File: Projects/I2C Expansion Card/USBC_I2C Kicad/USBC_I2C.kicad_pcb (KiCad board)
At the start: 2 copper layers, 26 x 30 mm, 12 parts, among them U1 MCP2221A

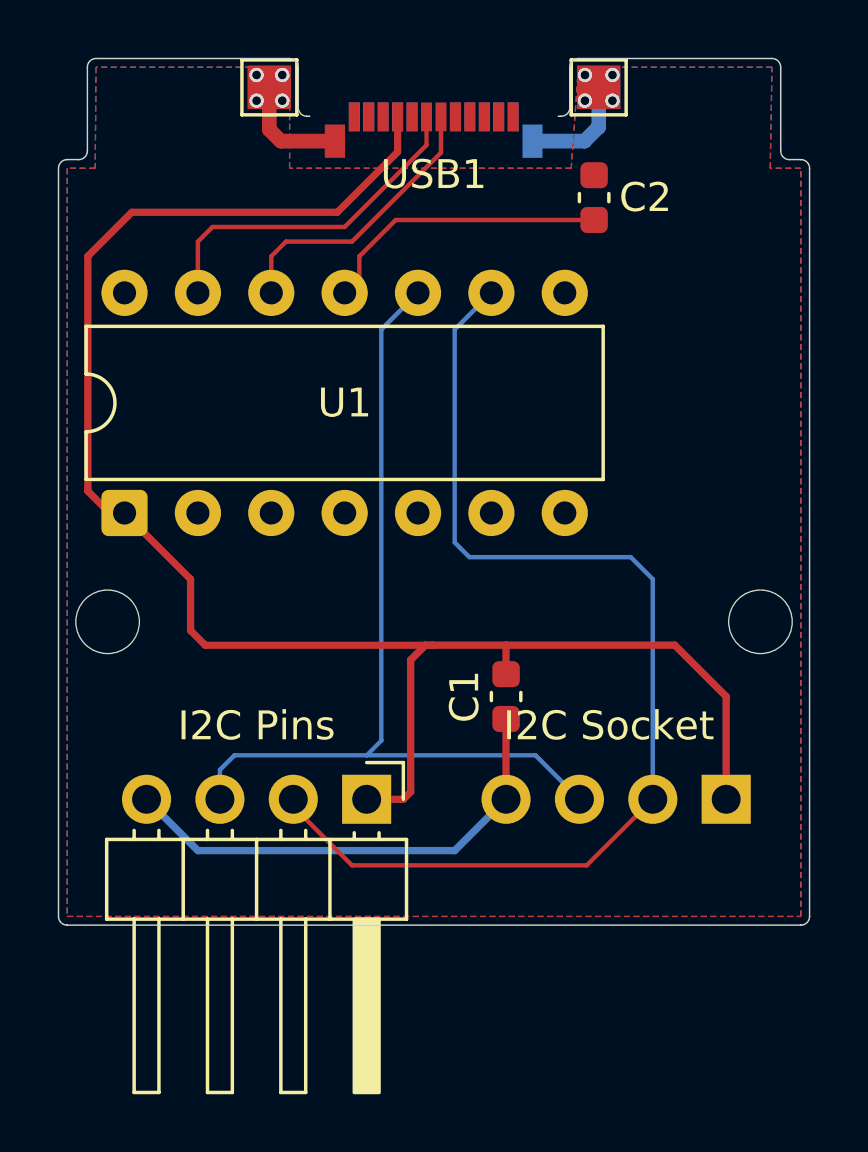
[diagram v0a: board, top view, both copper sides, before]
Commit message: Swapped to SMD chip
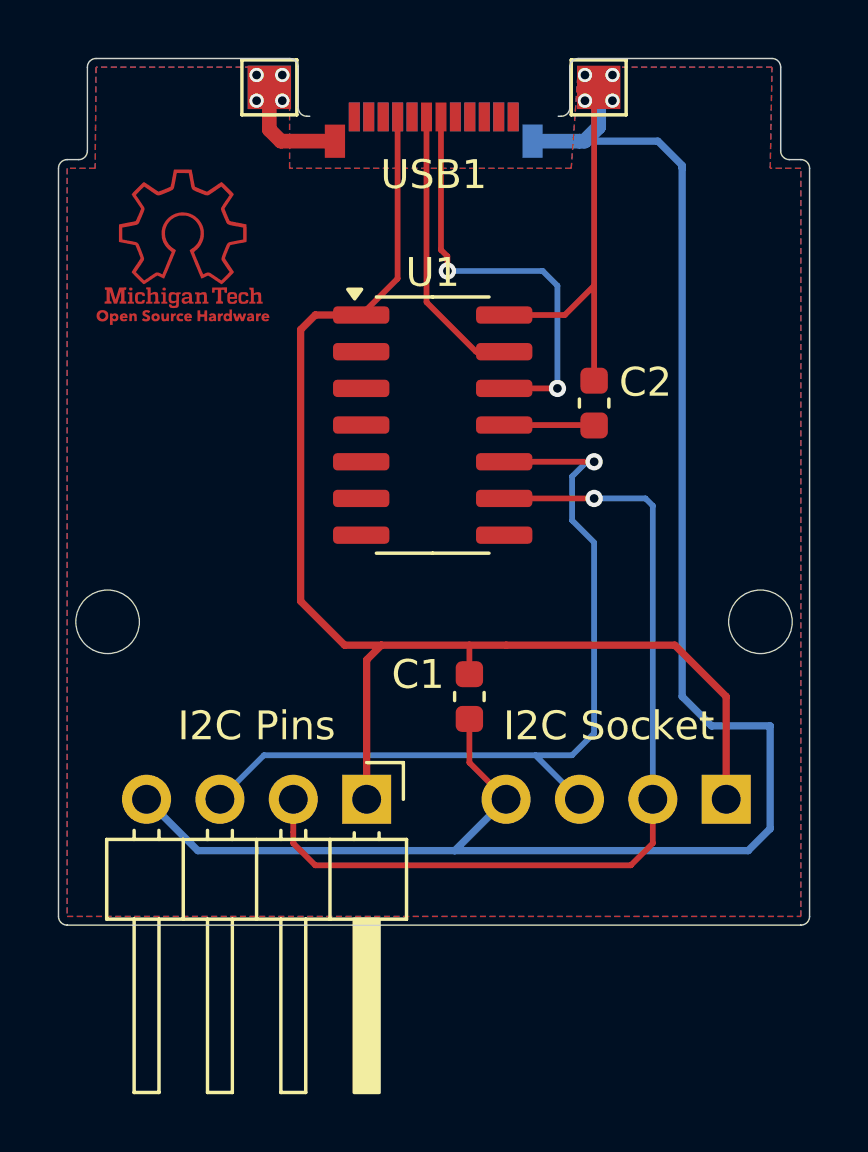
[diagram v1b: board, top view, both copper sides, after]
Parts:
- removed TP4: TestPoint, TestPoint:TestPoint_Pad_1.5x1.5mm
- added G***: LOGO, LOGO, F.Cu at (88.1, 63.8)
- U1: value MCP2221A -> MCP2221AxSL; footprint Package_DIP:DIP-14_W7.62mm -> Package_SO:SOIC-14_3.9x8.7mm_P1.27mm
- moved U1 11.1 mm to (96.8, 69.8), turned to 0 degrees
- moved C2 7.11 mm to (102.4, 69.1)
- moved C1 1.27 mm to (98.0, 79.2)
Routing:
- net GND: track 24.4 -> 79.2 mm
- net 5V: track 59.4 -> 45.3 mm
- net SDA: track 38.7 -> 31.5 mm, vias 0 -> 1
- net Net-(U1-VUSB): track 10.1 -> 3.12 mm
- net Net-(U1-D-): track 9.86 -> 14.8 mm, vias 0 -> 2
- net Net-(U1-D+): track 12.0 -> 9.81 mm
- net SCL: track 31.0 -> 29.3 mm, vias 0 -> 1

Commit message: Added capacitor values
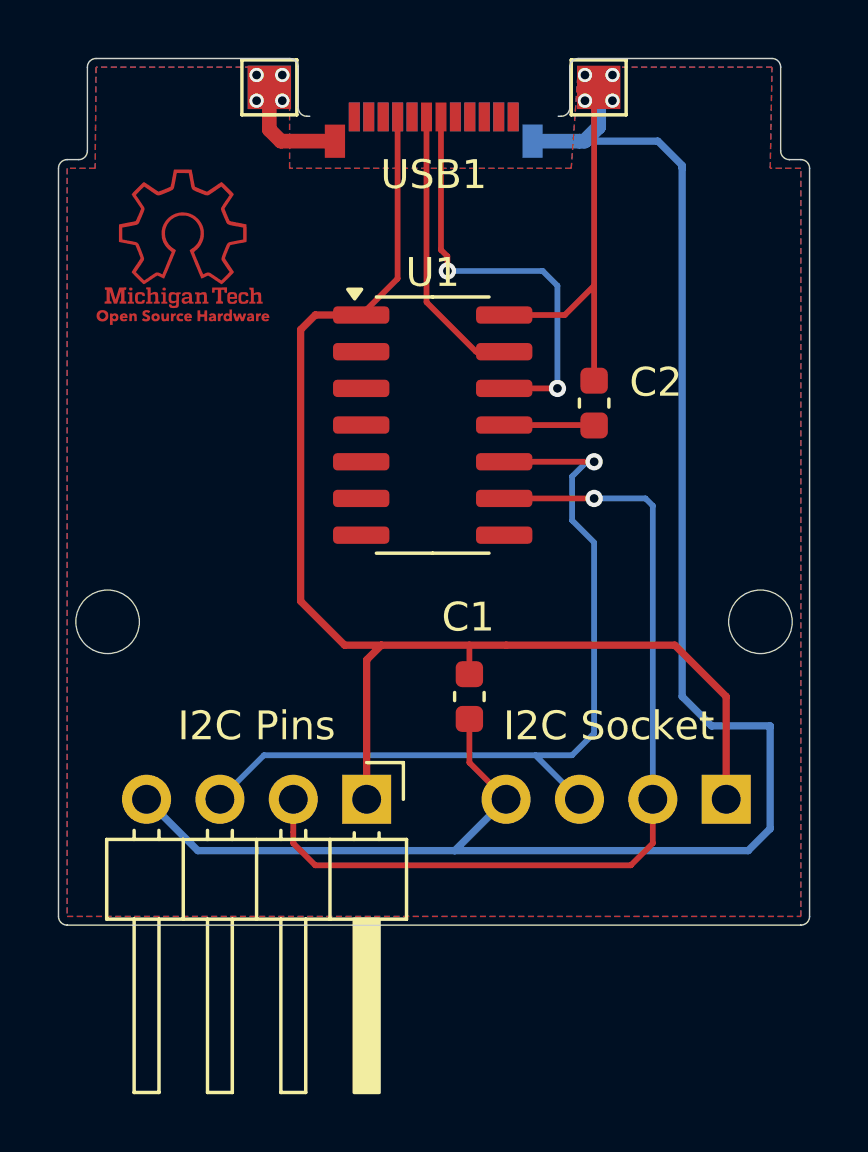
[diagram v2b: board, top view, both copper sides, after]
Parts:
- C1: value C -> .47uF
- C2: value C -> .22uF
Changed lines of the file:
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@@
 		(tags "capacitor")
 		(property "Reference" "C1"
-			(at 0.762 -1.778 180)
+			(at 2.748 -0.044 180)
 			(layer "F.SilkS")
 			(effects
@@
 			)
 		)
-		(property "Value" "C"
-			(at -0.762 -1.778 180)
+		(property "Value" ".47uF"
+			(at 0.748 -3.044 180)
 			(layer "F.Fab")
 			(effects
@@
 		(tags "capacitor")
 		(property "Reference" "C2"
-			(at -0.718 -1.778 0)
+			(at -0.718 -2.138 0)
 			(layer "F.SilkS")
 			(effects
@@
 			)
 		)
-		(property "Value" "C"
-			(at 0.762 -1.778 0)
-			(layer "F.Fab")
-			(effects
+		(property "Value" ".22uF"
+			(at 0.912 -3.138 0)
+			(layer "F.Fab")
+			(effects

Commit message: Added Impedance Matching and added 5V Plane
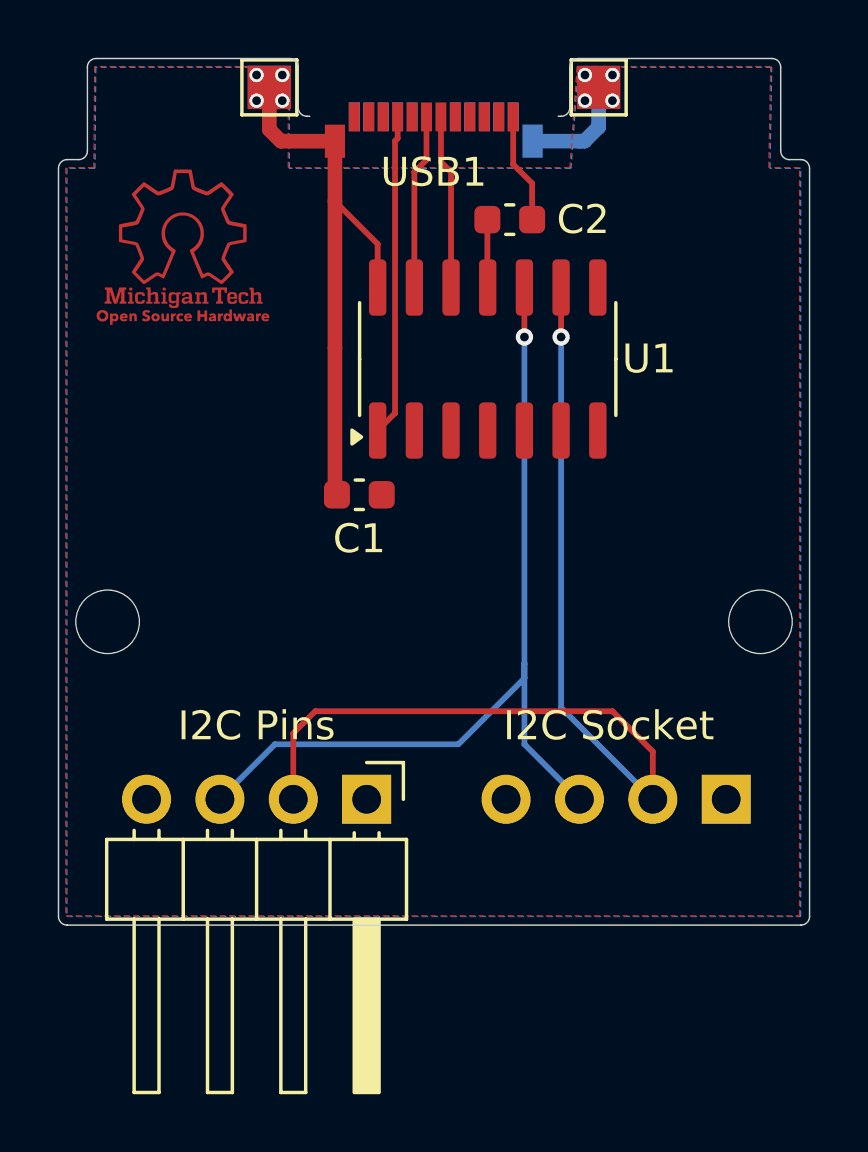
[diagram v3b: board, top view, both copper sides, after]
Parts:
- moved C1 7.96 mm to (94.2, 72.3), turned to 180 degrees
- moved C2 6.99 mm to (99.4, 62.7), turned to 180 degrees
- moved U1 2.98 mm to (98.7, 67.6), turned to 90 degrees
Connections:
- C1 pad 1: GND -> 5V
- C1 pad 2: 5V -> GND
- I2C Pins pad 1: (no net) -> 5V
- I2C Pins pad 2: (no net) -> SDA
- I2C Pins pad 3: (no net) -> SCL
- I2C Pins pad 4: (no net) -> GND
- I2C Socket pad 1: (no net) -> 5V
- I2C Socket pad 2: (no net) -> SDA
- I2C Socket pad 3: (no net) -> SCL
- I2C Socket pad 4: (no net) -> GND
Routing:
- net GND: track 79.2 -> 27.9 mm
- net 5V: track 45.3 -> 11.1 mm
- net Net-(U1-D-): track 14.8 -> 6.05 mm, vias 2 -> 0
- net SDA: track 31.5 -> 36.3 mm
- net Net-(U1-D+): track 9.81 -> 6.08 mm
- net SCL: track 29.3 -> 31.3 mm
- net Net-(U1-VUSB): track 3.12 -> 2.36 mm
- added copper zone on F.Cu, net 5V
- removed copper zone on F.Cu, net GND

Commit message: Fixed trace routing on dual output card
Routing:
- net SCL: track 31.3 -> 34.3 mm
- net SDA: track 36.3 -> 37.6 mm
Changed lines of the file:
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@@
 	)
 	(segment
-		(start 99.949 78.613)
-		(end 99.949 78.105)
+		(start 91.313 80.899)
+		(end 89.408 82.804)
 		(width 0.2)
 		(layer "B.Cu")
@@
 	)
 	(segment
-		(start 99.949 78.105)
-		(end 99.949 80.899)
+		(start 103.5 77.5)
+		(end 100.101 80.899)
 		(width 0.2)
 		(layer "B.Cu")
@@
 	)
 	(segment
-		(start 89.408 82.804)
-		(end 91.313 80.899)
+		(start 103.5 68.5)
+		(end 103.5 77.5)
 		(width 0.2)
 		(layer "B.Cu")
@@
 	)
 	(segment
-		(start 97.663 80.899)
-		(end 99.949 78.613)
+		(start 99.949 67.449)
+		(end 100.5 68)
+		(width 0.2)
+		(layer "B.Cu")
+		(net 7)
+	)
+	(segment
+		(start 99.949 66.802)
+		(end 99.949 67.449)
+		(width 0.2)
+		(layer "B.Cu")
+		(net 7)
+	)
+	(segment
+		(start 103 68)
+		(end 103.5 68.5)
+		(width 0.2)
+		(layer "B.Cu")
+		(net 7)
+	)
+	(segment
+		(start 100.101 80.899)
+		(end 91.313 80.899)
 		(width 0.2)
 		(layer "B.Cu")
@@
 	)
 	(segment
-		(start 91.313 80.899)
-		(end 97.663 80.899)
-		(width 0.2)
-		(layer "B.Cu")
-		(net 7)
-	)
-	(segment
-		(start 99.949 66.802)
-		(end 99.949 78.105)
+		(start 100.5 68)
+		(end 103 68)
 		(width 0.2)
 		(layer "B.Cu")
@@
 	)
 	(segment
-		(start 101.219 79.629)
+		(start 103.302 66.802)
+		(end 104.5 68)
+		(width 0.2)
+		(layer "B.Cu")
+		(net 9)
+	)
+	(segment
+		(start 104.5 68)
+		(end 104.5 82.698)
+		(width 0.2)
+		(layer "B.Cu")
+		(net 9)
+	)
+	(segment
+		(start 104.5 82.698)
 		(end 104.394 82.804)
 		(width 0.2)
@@
 	(segment
 		(start 101.219 66.802)
-		(end 101.219 79.629)
+		(end 103.302 66.802)
 		(width 0.2)
 		(layer "B.Cu")

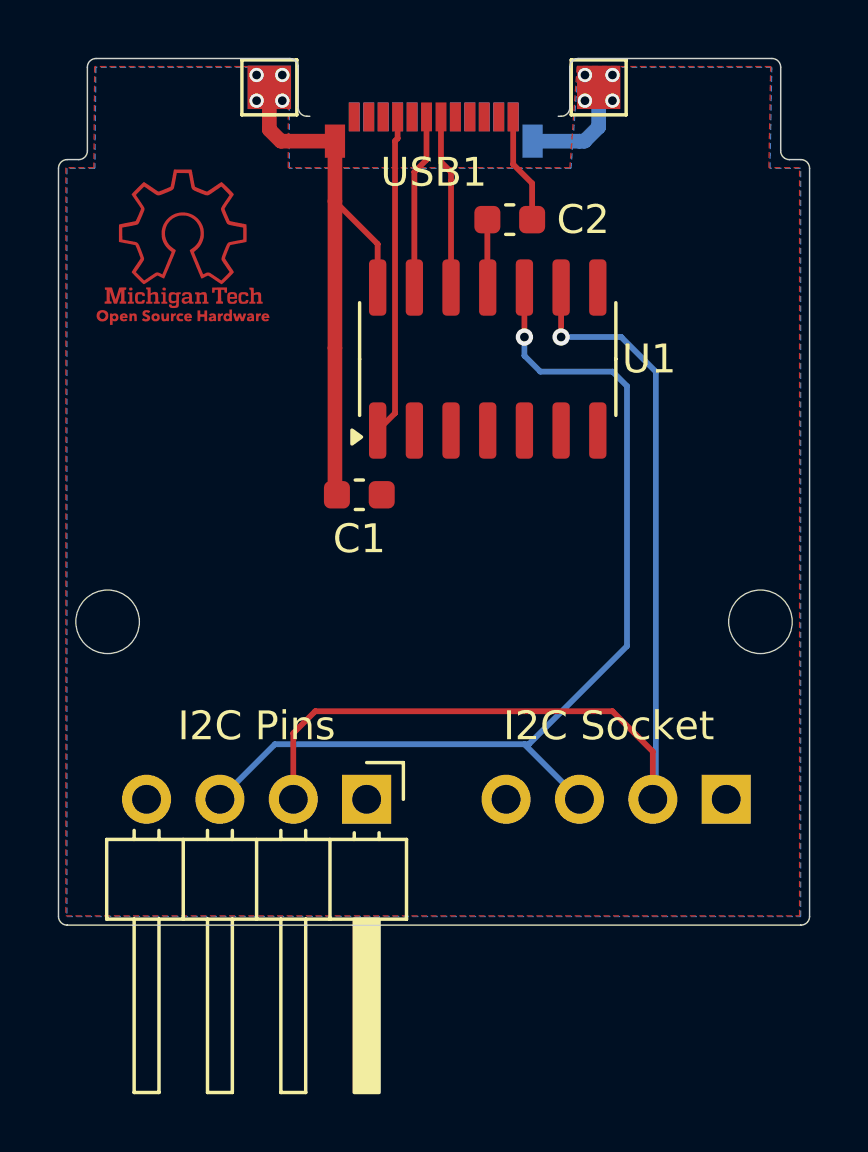
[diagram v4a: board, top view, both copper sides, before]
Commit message: Reworked pcb to put everything on one board
Merged the 3 versions into one, added through hole cap holes, added uart switch, fixed the pcb edge
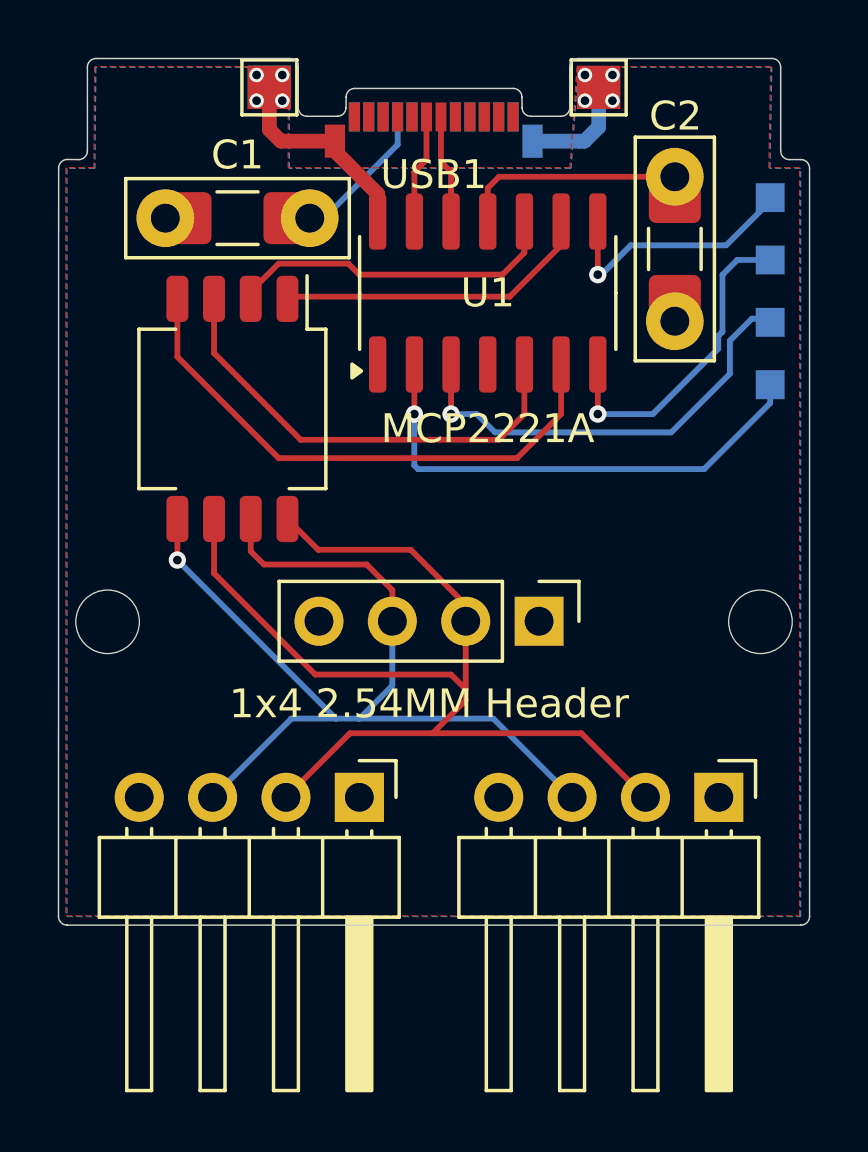
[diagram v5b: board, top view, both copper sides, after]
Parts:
- removed G***: LOGO, LOGO
- removed I2C Pins: I2C Pins, Connector_PinHeader_2.54mm:PinHeader_1x04_P2.54mm_Horizontal
- removed I2C Socket: PinSocket_1x04_P2.54mm_Horizontal, Connector_PinSocket_2.54mm:PinSocket_1x04_P2.54mm_Horizontal
- added REF**: PinHeader_1x04_P2.54mm_Horizontal, Connector_PinHeader_2.54mm:PinHeader_1x04_P2.54mm_Horizontal, F.Cu at (94.2, 82.7)
- added REF**: TestPoint_Pad_1.0x1.0mm, TestPoint:TestPoint_Pad_1.0x1.0mm, B.Cu at (108.5, 64.1)
- added REF**: C_Disc_D7.5mm_W2.5mm_P5.00mm, Capacitor_THT:C_Disc_D7.5mm_W2.5mm_P5.00mm, F.Cu at (92.5, 62.7)
- added REF**: SW_DIP_SPSTx04_Slide_Copal_CHS-04B_W7.62mm_P1.27mm, Button_Switch_SMD:SW_DIP_SPSTx04_Slide_Copal_CHS-04B_W7.62mm_P1.27mm, F.Cu at (89.8, 69.3)
- added REF**: PinHeader_1x04_P2.54mm_Vertical, Connector_PinHeader_2.54mm:PinHeader_1x04_P2.54mm_Vertical, F.Cu at (100.5, 76.6)
- added REF**: C_Disc_D7.5mm_W2.5mm_P5.00mm, Capacitor_THT:C_Disc_D7.5mm_W2.5mm_P5.00mm, F.Cu at (105.2, 61.3)
- added REF**: PinHeader_1x04_P2.54mm_Horizontal, Connector_PinHeader_2.54mm:PinHeader_1x04_P2.54mm_Horizontal, F.Cu at (106.7, 82.7)
- added REF**: TestPoint_Pad_1.0x1.0mm, TestPoint:TestPoint_Pad_1.0x1.0mm, B.Cu at (108.5, 62.0)
- added REF**: TestPoint_Pad_1.0x1.0mm, TestPoint:TestPoint_Pad_1.0x1.0mm, B.Cu at (108.5, 68.5)
- added REF**: TestPoint_Pad_1.0x1.0mm, TestPoint:TestPoint_Pad_1.0x1.0mm, B.Cu at (108.5, 66.3)
- C1: value .47uF -> 0.47uF; footprint Capacitor_SMD:C_0603_1608Metric -> Capacitor_SMD:C_1206_3216Metric_Pad1.33x1.80mm_HandSolder
- C2: value .22uF -> 0.22uF; footprint Capacitor_SMD:C_0603_1608Metric -> Capacitor_SMD:C_1206_3216Metric_Pad1.33x1.80mm_HandSolder
- U1: value MCP2221AxSL -> MCP2221A
- moved C1 10.5 mm to (90.0, 62.7), turned to 0 degrees
- moved C2 5.80 mm to (105.2, 63.8), turned to 90 degrees
- moved U1 2.29 mm to (98.7, 65.3)
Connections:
- C1 pad 1: 5V -> GND
- C1 pad 2: GND -> 5V
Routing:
- net (no net): track 0.00 -> 74.2 mm, vias 0 -> 1
- net SDA: track 37.6 -> 11.1 mm, vias 1 -> 0
- net SCL: track 34.3 -> 11.7 mm, vias 1 -> 0
- net unconnected-(U1-UTx-Pad6): track 0.00 -> 19.1 mm
- net Net-(D1-A): track 0.00 -> 17.7 mm, vias 0 -> 1
- net unconnected-(U1-URx-Pad5): track 0.00 -> 15.9 mm
- net GND: track 27.9 -> 12.3 mm
- net Net-(D2-A): track 0.00 -> 15.3 mm, vias 0 -> 1
- net Net-(D3-A): track 0.00 -> 11.3 mm, vias 0 -> 1
- net Net-(D4-A): track 0.00 -> 8.86 mm, vias 0 -> 1
- net Net-(U1-VUSB): track 2.36 -> 10.0 mm
- net 5V: track 11.1 -> 6.45 mm
- net Net-(U1-D+): track 6.08 -> 3.80 mm
- net Net-(U1-D-): track 6.05 -> 3.77 mm
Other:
- outline, holes or cut-outs redrawn
- board text added: "1x4 2.54MM Header"
- board text removed: "${REFERENCE}"

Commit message: Added jumpers in case switch doesnt work
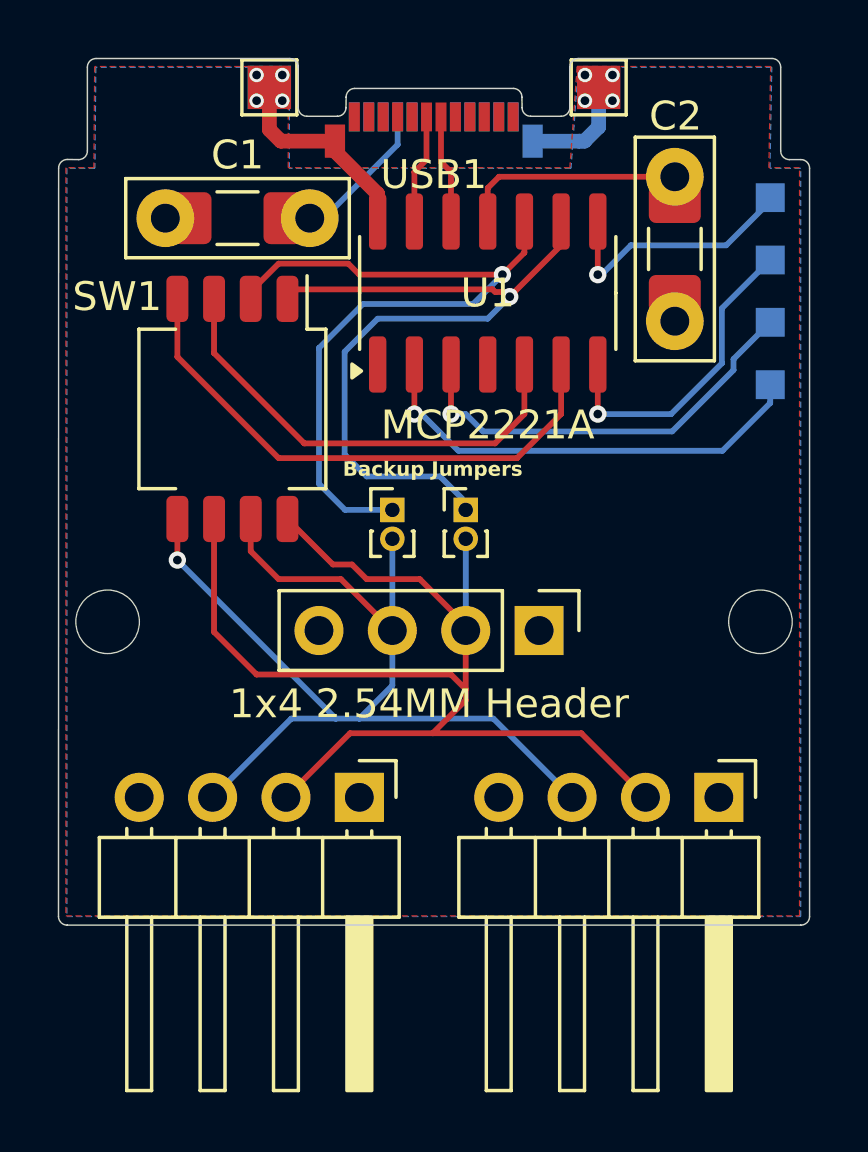
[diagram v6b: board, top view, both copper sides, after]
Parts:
- added REF**: PinHeader_1x02_P1.00mm_Vertical, Connector_PinHeader_1.00mm:PinHeader_1x02_P1.00mm_Vertical, F.Cu at (95.4, 72.8)
- added REF**: PinHeader_1x02_P1.00mm_Vertical, Connector_PinHeader_1.00mm:PinHeader_1x02_P1.00mm_Vertical, F.Cu at (97.9, 72.8)
- moved REF** 0.32 mm to (100.5, 77.0)
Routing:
- net SDA: track 11.1 -> 26.5 mm, vias 0 -> 1
- net SCL: track 11.7 -> 26.7 mm, vias 0 -> 1
- net (no net): track 74.2 -> 80.2 mm
- net Net-(D1-A): track 17.7 -> 16.1 mm
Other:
- board text added: "Backup Jumpers"
- board text added: "SW1"
